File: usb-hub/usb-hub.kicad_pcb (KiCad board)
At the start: 2 copper layers, 42 x 43 mm, 56 parts, among them J5 USB_A, J7 USB_C_Receptacle, J8 USB_C_Receptacle, P1 CONN_01X04, P2 CONN_02X03, U1 usb-2412, U2 LD1117S12TR_SOT223, U3 rgbled, U4 ATmega32U4, U5 24LC16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

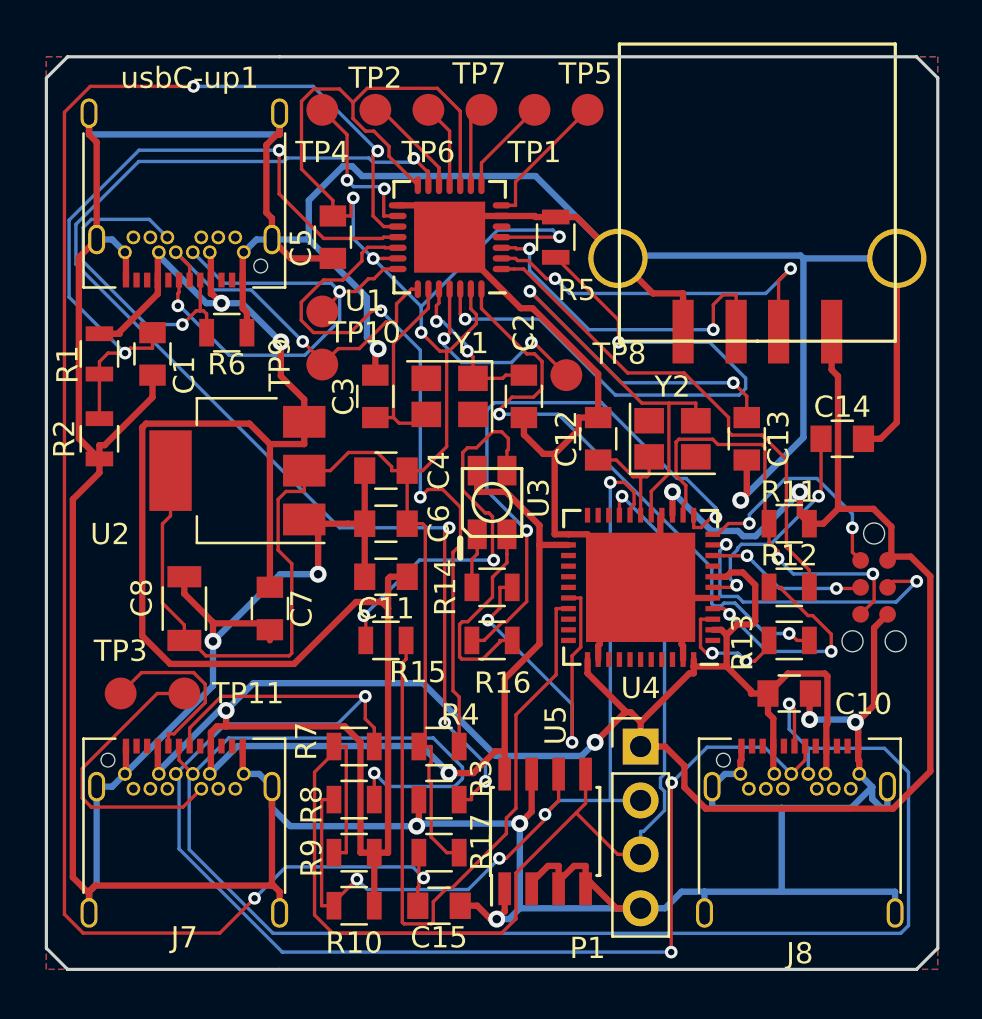
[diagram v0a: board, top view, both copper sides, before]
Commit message: switched to smt usbc plugs and added power switching for both sockets
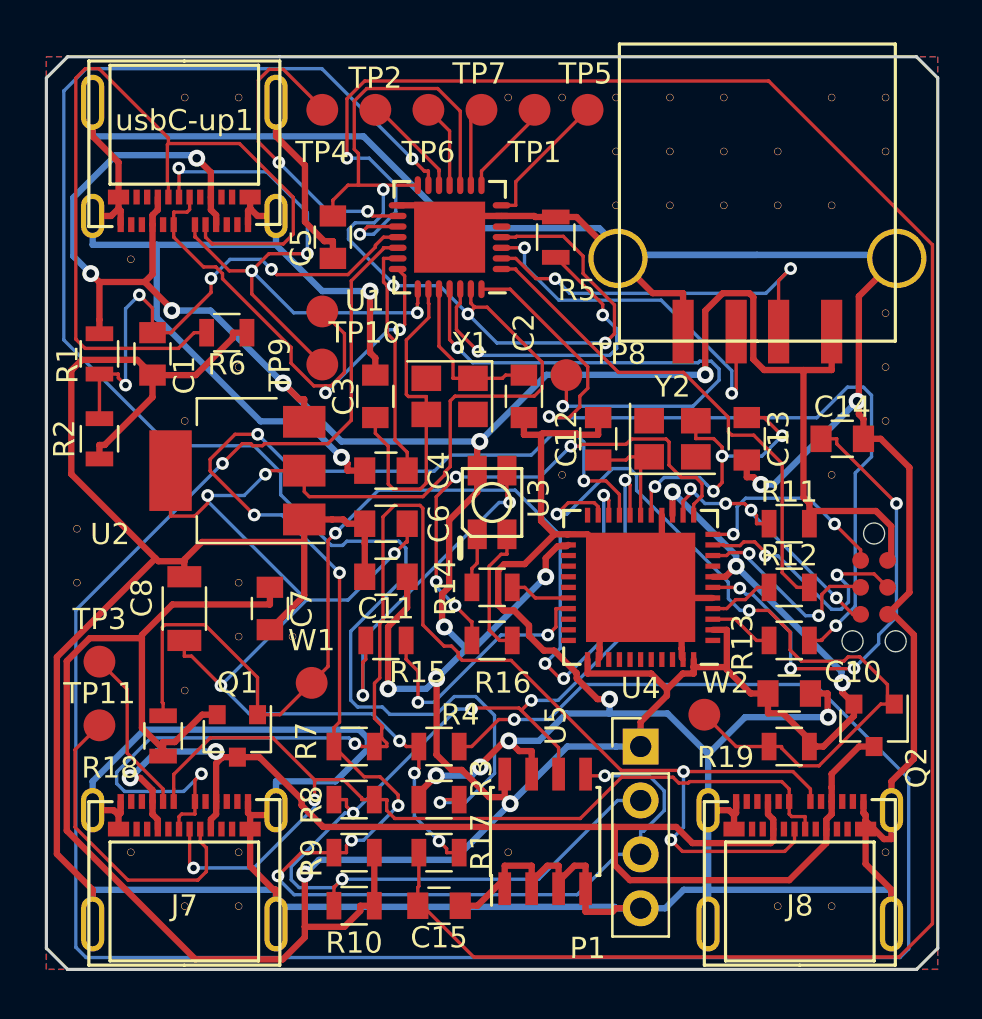
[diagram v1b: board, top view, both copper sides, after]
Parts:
- removed svg2mod: G***, fp:dygma-logo
- added Q1: Q_PMOS_GSD, TO_SOT_Packages_SMD:SOT-23, F.Cu at (118.0, 110.0)
- added Q2: Q_PMOS_GSD, TO_SOT_Packages_SMD:SOT-23, F.Cu at (148.0, 109.5)
- added R18: 10k, Resistors_SMD:R_0805, F.Cu at (114.5, 110.0)
- added R19: 10k, Resistors_SMD:R_0805, F.Cu at (144.0, 110.5)
- added V10_10: AUTO_VIA, VIA_MATRIX, F.Cu at (133.3, 97.7)
- added V10_3: AUTO_VIA, VIA_MATRIX, F.Cu at (133.3, 79.9)
- added V11_3: AUTO_VIA, VIA_MATRIX, F.Cu at (135.8, 79.9)
- added V11_4: AUTO_VIA, VIA_MATRIX, F.Cu at (135.8, 82.5)
- added V11_5: AUTO_VIA, VIA_MATRIX, F.Cu at (135.8, 85.0)
- added V12_3: AUTO_VIA, VIA_MATRIX, F.Cu at (138.4, 79.9)
- added V12_4: AUTO_VIA, VIA_MATRIX, F.Cu at (138.4, 82.5)
- added V12_5: AUTO_VIA, VIA_MATRIX, F.Cu at (138.4, 85.0)
- added V13_3: AUTO_VIA, VIA_MATRIX, F.Cu at (140.9, 79.9)
- added V13_4: AUTO_VIA, VIA_MATRIX, F.Cu at (140.9, 82.5)
- added V13_5: AUTO_VIA, VIA_MATRIX, F.Cu at (140.9, 85.0)
- added V14_18: AUTO_VIA, VIA_MATRIX, F.Cu at (143.5, 118.0)
- added V14_4: AUTO_VIA, VIA_MATRIX, F.Cu at (143.5, 82.5)
- added V14_5: AUTO_VIA, VIA_MATRIX, F.Cu at (143.5, 85.0)
- added V15_10: AUTO_VIA, VIA_MATRIX, F.Cu at (146.0, 97.7)
- added V15_18: AUTO_VIA, VIA_MATRIX, F.Cu at (146.0, 118.0)
- added V15_3: AUTO_VIA, VIA_MATRIX, F.Cu at (146.0, 79.9)
- added V15_5: AUTO_VIA, VIA_MATRIX, F.Cu at (146.0, 85.0)
- added V16_17: AUTO_VIA, VIA_MATRIX, F.Cu at (148.5, 115.5)
- added V16_3: AUTO_VIA, VIA_MATRIX, F.Cu at (148.5, 79.9)
- added V16_4: AUTO_VIA, VIA_MATRIX, F.Cu at (148.5, 82.5)
- added V16_7: AUTO_VIA, VIA_MATRIX, F.Cu at (148.5, 90.1)
- added V16_8: AUTO_VIA, VIA_MATRIX, F.Cu at (148.5, 92.6)
- added V16_9: AUTO_VIA, VIA_MATRIX, F.Cu at (148.5, 95.2)
- added V1_11: AUTO_VIA, VIA_MATRIX, F.Cu at (110.4, 100.2)
- added V1_12: AUTO_VIA, VIA_MATRIX, F.Cu at (110.4, 102.8)
- added V2_17: AUTO_VIA, VIA_MATRIX, F.Cu at (113.0, 115.5)
- added V2_6: AUTO_VIA, VIA_MATRIX, F.Cu at (113.0, 87.5)
- added V3_14: AUTO_VIA, VIA_MATRIX, F.Cu at (115.5, 107.9)
- added V3_18: AUTO_VIA, VIA_MATRIX, F.Cu at (115.5, 118.0)
- added V3_3: AUTO_VIA, VIA_MATRIX, F.Cu at (115.5, 79.9)
- added V3_9: AUTO_VIA, VIA_MATRIX, F.Cu at (115.5, 95.2)
- added V4_12: AUTO_VIA, VIA_MATRIX, F.Cu at (118.1, 102.8)
- added V4_13: AUTO_VIA, VIA_MATRIX, F.Cu at (118.1, 105.3)
- added V4_17: AUTO_VIA, VIA_MATRIX, F.Cu at (118.1, 115.5)
- added V4_18: AUTO_VIA, VIA_MATRIX, F.Cu at (118.1, 118.0)
- added V4_3: AUTO_VIA, VIA_MATRIX, F.Cu at (118.1, 79.9)
- added V4_8: AUTO_VIA, VIA_MATRIX, F.Cu at (118.1, 92.6)
- added V5_13: AUTO_VIA, VIA_MATRIX, F.Cu at (120.6, 105.3)
- added V9_17: AUTO_VIA, VIA_MATRIX, F.Cu at (130.8, 115.5)
- added V9_3: AUTO_VIA, VIA_MATRIX, F.Cu at (130.8, 79.9)
- added W1: TEST_1P, Measurement_Points:Measurement_Point_Round-SMD-Pad_Small, F.Cu at (121.5, 107.5)
- added W2: TEST_1P, Measurement_Points:Measurement_Point_Round-SMD-Pad_Small, F.Cu at (140.0, 109.0)
- J7, J8, usbC-up1: footprint Connectors_USB:USB_C_Receptacle_Amphenol_12401548E4-2A -> fp:usb-c-24smt
- moved TP11 4.27 mm to (111.5, 109.5)
- moved J7 2.00 mm to (115.5, 113.5)
- moved J8 2.00 mm to (144.5, 113.5)
- moved usbC-up1 2.00 mm to (115.5, 85.5)
- moved TP3 1.80 mm to (111.5, 106.5)
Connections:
- J7 pad A4: +5V -> +5C
- J7 pad A9: +5V -> +5C
- J7 pad B4: +5V -> +5C
- J7 pad B9: +5V -> +5C
- J8 pad A4: +5V -> +5C
- J8 pad A9: +5V -> +5C
- J8 pad B4: +5V -> +5C
- J8 pad B9: +5V -> +5C
- U4 pad 20: Net-(U4-Pad20) -> /huble/left-switch
- U4 pad 21: Net-(U4-Pad21) -> /huble/right-switch
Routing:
- net Net-(R4-Pad2): track 34.6 -> 113.9 mm
- net Earth: track 352.0 -> 419.0 mm
- net +5C: track 0.00 -> 60.3 mm, vias 0 -> 2
- net /huble/left-switch: track 0.00 -> 52.5 mm, vias 0 -> 4
- net /huble/right-switch: track 0.00 -> 37.0 mm, vias 0 -> 2
- net /huble/usbc-dp: track 79.4 -> 46.7 mm
- net Net-(R6-Pad1): track 15.8 -> 41.4 mm, vias 1 -> 0
- net /huble/sda: track 56.1 -> 79.0 mm, vias 1 -> 8
- net Net-(C15-Pad1): track 80.4 -> 102.6 mm, vias 4 -> 2
- net +3V3: track 107.3 -> 128.6 mm, vias 4 -> 11
- net /huble/pwm_g: track 32.8 -> 12.6 mm, vias 0 -> 2
- net Net-(R3-Pad2): track 58.1 -> 75.8 mm, vias 4 -> 2
- net Net-(TP8-Pad1): track 9.87 -> 25.6 mm
- net Net-(C13-Pad1): track 29.7 -> 14.4 mm, vias 2 -> 4
- net /usb-up-p: track 17.8 -> 32.6 mm, vias 1 -> 4
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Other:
- net class Default: clearance 0.15 -> 0.16
- net class power: clearance 0.15 -> 0.16
- rule trace_clearance: 0.15 -> 0.16
- board text added: "$ver$ "5182b8b" 2018-01-23"
- board text removed: "$ver$ "8c3a289" 2018-01-18"

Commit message: fixed a track bug
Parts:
- added svg2mod: G***, fp:dygma-logo, B.Cu at (128.0, 99.5)
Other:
- board text added: "$ver$ "4fd924d" 2018-01-25"
- board text removed: "$ver$ "5182b8b" 2018-01-23"
